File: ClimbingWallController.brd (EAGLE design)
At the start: 100 x 80 mm, 339 parts, among them IC1 74HCT138D, IC2 74HCT138D, IC3 PIC24FJ32GB004, IC4 SN74LV4052AD, IC5 SN74LV4052AD, IC6 TC1015, IC7 NCP1117, J1 PWR, Q1 DPBT8105, Q10 DPBT8105, Q11 DPBT8105, Q12 DPBT8105, Q13 DPBT8105, Q14 DPBT8105, Q15 DPBT8105, Q16 DPBT8105, Q17 NC, Q2 DPBT8105, Q3 DPBT8105, Q4 DPBT8105, Q5 DPBT8105, Q6 DPBT8105, Q7 DPBT8105, Q8 DPBT8105, Q9 DPBT8105, X1 MINI-USB-32005-201

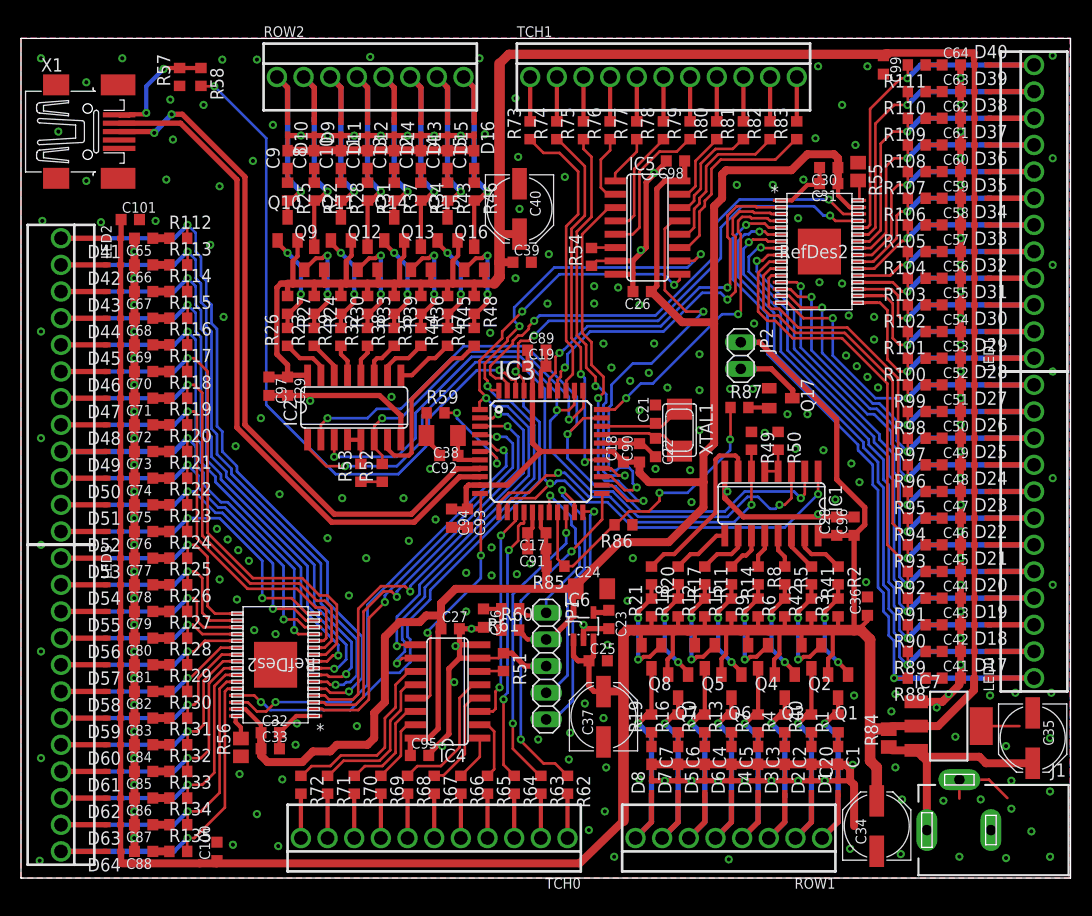
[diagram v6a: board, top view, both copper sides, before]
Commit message: DRC Passed with SEEED Rules. Added extra input to touch connector because 11-socket parts aren't available. Fixed 5v regulator pin out, and added PCB heat sink. Messed with device attributes for manufacturer part number. Exported BOM. (Awaiting clean up for BOM commit).
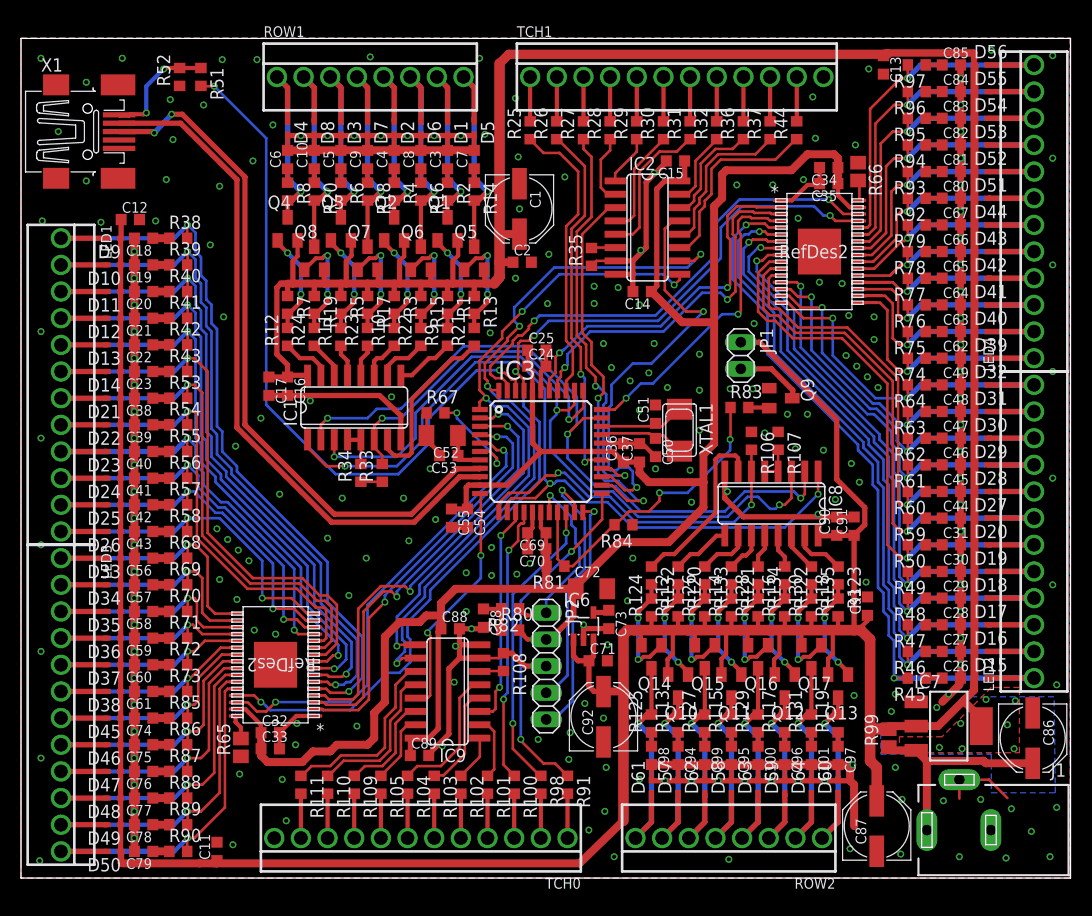
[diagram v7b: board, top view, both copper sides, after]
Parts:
- removed LED0: (no value), Parts:OSTVN12
- added LED4: (no value), Parts:OSTVN12
- C1: value 22n -> 100uF; device resistor:C0603 -> resistor:PANASONIC_D
- C10, C3, C4, C5, C6, C7, C8, C9: device resistor:C0603 -> resistor:C0603K
- C100, C101, C99: value 0.1uF -> 22n; device rcl:C0603K -> resistor:C0603K
- C11, C12, C13, C14: value 22n -> 0.1uF; device resistor:C0603 -> rcl:C0603K
- C15: value 22n -> NC; device resistor:C0603 -> rcl:C0603K
- C16, C90: value NC -> 0.1uF
- C17: value 0.1uF -> NC
- C18, C19, C26, C27, C28, C29, C31: value 0.1uF -> 1n; device rcl:C0603K -> resistor:C0603K
- C2: value 22n -> 1uF; device resistor:C0603 -> rcl:C0603K
- C20: value 22n -> 1n; device resistor:C0603 -> resistor:C0603K
- C21, C22: value NC -> 1n; device rcl:C0603K -> resistor:C0603K
- C23: value 470pF -> 1n; device rcl:C0603K -> resistor:C0603K
- C24: value 10uF -> 0.1uF; device rcl:C1206K -> rcl:C0603K
- C25: value 1uF -> NC
- C30, C39: value 1uF -> 1n; device rcl:C0603K -> resistor:C0603K
- C34: value 100uF -> 1uF; device resistor:PANASONIC_D -> rcl:C0603K
- C35: value 100uF -> 0.1uF; device resistor:PANASONIC_D -> rcl:C0603K
- C36: value 1uF -> 0.1uF
- C37: value 100uF -> NC; device resistor:PANASONIC_D -> rcl:C0603K
- C38: value 10uF -> 1n; device rcl:C1206K -> resistor:C0603K
- C40: value 100uF -> 1n; device resistor:PANASONIC_D -> resistor:C0603K
- C50, C51, C53, C55, C68, C70: value 1n -> NC; device resistor:C0603K -> rcl:C0603K
- C52, C72: value 1n -> 10uF; device resistor:C0603K -> rcl:C1206K
- C54, C69, C88: value 1n -> 0.1uF; device resistor:C0603K -> rcl:C0603K
- C71: value 1n -> 1uF; device resistor:C0603K -> rcl:C0603K
- C73: value 1n -> 470pF; device resistor:C0603K -> rcl:C0603K
- C86, C87: value 1n -> 100uF; device resistor:C0603K -> resistor:PANASONIC_D
- C92: value NC -> 100uF; device rcl:C0603K -> resistor:PANASONIC_D
- C93: value 0.1uF -> 1uF
- C94, C95, C96, C97, C98: value NC -> 22n; device rcl:C0603K -> resistor:C0603K
- IC2: value 74HCT138D -> SN74LV4052AD
- IC4, IC5: value SN74LV4052AD -> TLC5952; device Parts:SO16 -> Parts:HTSSOP-32POWERPAD
- IC7: value NCP1117 -> (none)
- IC8: value (none) -> 74HCT138D; device Parts:HTSSOP-32POWERPAD -> Parts:SO16
- IC9: value (none) -> SN74LV4052AD; device Parts:HTSSOP-32POWERPAD -> Parts:SO16
- J1: device con-jack:DCJ0303 -> Parts:DCJ0303
- JP1: value DEBUG -> BUZZER; device pinhead:1X05 -> pinhead:1X02
- JP2: value BUZZER -> DEBUG; device pinhead:1X02 -> pinhead:1X05
- Q17: value NC -> DPBT8105; device transistor:SOT23-EBC -> Parts:SOT23
- Q9: value DPBT8105 -> NC; device Parts:SOT23 -> transistor:SOT23-EBC
- R1, R13, R19, R7: value 20 -> NC
- R10, R22: value 20 -> 750
- R100, R101, R102, R103, R104, R105, R109, R110, R111, R91, R98: value 300 -> 390
- R106, R107, R108: value 300 -> 4.7k
- R112, R114, R116, R118, R124, R126, R128, R130: value 300 -> NC
- R113, R115, R117, R119, R125, R127, R129, R131: value 300 -> 20
- R12, R21, R24, R9: value NC -> 750
- R120, R121, R122, R123, R132, R133, R134, R135: value 300 -> 750
- R14, R2, R20, R8: value 750 -> 20
- R17, R5: value 750 -> NC
- R18, R6: value NC -> 20
- R25, R28, R31, R37: value 20 -> 390
- R26, R29, R32, R44: value 750 -> 390
- R27, R30, R36: value NC -> 390
- R33: value NC -> 4.7k
- R34: value 20 -> 4.7k
- R35: value 750 -> 4.7k
- R38, R41, R47: value 750 -> 300
- R39, R42, R45, R48, R85, R86, R87: value NC -> 300
- R40, R43, R46: value 20 -> 300
- R49, R50, R53, R54, R57, R58, R59, R60: value 4.7k -> 300
- R55, R56: value 1.37k 0.5% -> 300; device resistor:R0805 -> Parts:R0603
- R61, R62, R63, R64, R68, R69, R70, R71, R72, R73, R74, R75, R76, R77, R78, R79: value 390 -> 300
- R65, R66: value 390 -> 1.37k 0.5%; device Parts:R0603 -> resistor:R0805
- R67, R80: value 390 -> 4.7k
- R81, R83: value 390 -> NC
- R84: value 0 -> NC; device resistor:R0805 -> Parts:R0603
- R99: value 300 -> 0; device Parts:R0603 -> resistor:R0805
- TCH0, TCH1: device Parts:OSTVN11 -> Parts:OSTVN12
- moved C85 102.2 mm to (88.6, 77.5), turned to 0 degrees
- moved D38 99.0 mm to (8.89, 17.8), turned to 180 degrees
- moved D56 99.0 mm to (91.4, 77.5), turned to 0 degrees
- moved C84 99.0 mm to (88.6, 74.9), turned to 0 degrees
- moved D55 96.3 mm to (91.4, 74.9), turned to 0 degrees
- moved D37 96.3 mm to (8.89, 20.3), turned to 180 degrees
- moved C83 95.9 mm to (88.6, 72.4), turned to 0 degrees
- moved LED1 94.2 mm to (3.81, 47.0), turned to 270 degrees
- moved D36 93.8 mm to (8.89, 22.9), turned to 180 degrees
- moved D54 93.8 mm to (91.4, 72.4), turned to 0 degrees
- moved LED2 93.8 mm to (96.5, 33.0), turned to 90 degrees
- moved C61 92.9 mm to (11.7, 17.8), turned to 180 degrees
- moved C82 92.9 mm to (88.6, 69.8), turned to 0 degrees
- moved D35 91.5 mm to (8.89, 25.4), turned to 180 degrees
- moved D53 91.5 mm to (91.4, 69.8), turned to 0 degrees
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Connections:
- removed net N$118 (its old number): C67.1, R114.1
- removed net N$66: R65.2, TCH0.4
- removed net N$68: R67.2, TCH0.6
- removed net N$70: R69.2, TCH0.8
- removed net N$72: R71.2, TCH0.10
- removed net N$74: R74.2, TCH1.2
- removed net N$75: R76.2, TCH1.4
- removed net N$76: R78.2, TCH1.6
- removed net N$77: R80.2, TCH1.8
- removed net N$78: R82.2, TCH1.10
- new net N$31: R98.2, TCH0.2
- new net N$32: R101.2, TCH0.4
- new net N$34: C101.1, R131.1
- new net N$35: R103.2, TCH0.6
- new net N$36: R105.2, TCH0.8
- new net N$37: R110.2, TCH0.10
- new net N$38: R26.2, TCH1.2
- new net N$39: R28.2, TCH1.4
- new net N$40: R30.2, TCH1.6
- new net N$49: R37.2, TCH1.10
- net +3V3: now also C14.1, C15.1, C25.1, C34.1, C35.1, C36.1, C37.1, C54.1, C55.1, C69.1, C70.1, C72.1, C88.1, IC2.16, IC4.31, IC5.31, IC9.16, JP2.2, R80.2, R81.2; no longer C17.1, C18.1, C19.1, C26.1, C27.1, C30.1, C31.1, C90.1, C91.1, C93.1, C94.1, C95.1, C98.1, IC4.16, IC5.16, IC8.31, IC9.31, JP1.2, R60.2, R85.2
- net +5V: now also C1.+, C11.1, C12.1, C13.1, C16.1, C17.1, C2.1, C71.1, C87.+, C90.1, C91.1, C92.+, C93.1, D10.C, D11.C, D12.C, D13.C, D14.C, D15.C, D16.C, D9.C, IC7.4, IC8.16, JP1.1, Q17.2, R1.1, R112.1, R114.1, R116.1, R118.1, R124.1, R126.1, R128.1, R13.1, R130.1, R17.1, R19.1, R5.1, R7.1, R99.2; no longer C100.1, C101.1, C25.1, C28.1, C29.1, C34.+, C36.1, C37.+, C39.1, C40.+, C96.1, C97.1, C99.1, D57.C, D58.C, D59.C, D60.C, D61.C, D62.C, D63.C, D64.C, IC2.16, JP2.1, Q9.2, R12.1, R18.1, R21.1, R24.1, R27.1, R30.1, R33.1, R36.1, R39.1, R42.1, R45.1, R48.1, R6.1, R84.2, R9.1
- net AMSEL0: now also IC2.10, IC9.10; no longer IC4.10, IC5.10
- net AMSEL1: now also IC2.9, IC9.9; no longer IC4.9, IC5.9
- net B0: now also D17.A, IC5.7, LED2.3, R47.2; no longer D19.A, IC8.7, LED0.3, R90.2
- net B1: now also D20.A, IC5.10, LED2.6, R50.2; no longer D22.A, IC8.10, LED0.6, R93.2
- net B10: now also D23.A, IC4.13, LED1.9, R55.2; no longer D49.A, IC9.13, LED2.9, R120.2
- net B11: now also D26.A, IC4.16, LED1.12, R58.2; no longer D52.A, IC9.16, LED2.12, R123.2
- net B12: now also D35.A, IC4.19, R70.2; no longer D55.A, IC9.19, R126.2
- net B13: now also D38.A, IC4.22, R73.2; no longer D58.A, IC9.22, R129.2
- net B14: now also D47.A, IC4.25, R87.2; no longer D61.A, IC9.25, R132.2
- net B15: now also D50.A, IC4.28, R90.2; no longer D64.A, IC9.28, R135.2
- net B2: now also D29.A, IC5.13, LED2.9, R61.2; no longer D25.A, IC8.13, LED0.9, R96.2
- net B3: now also D32.A, IC5.16, LED2.12, R64.2; no longer D28.A, IC8.16, LED0.12, R99.2
- net B4: now also D41.A, IC5.19, LED4.3, R76.2; no longer D31.A, IC8.19, LED1.3, R102.2
- net B5: now also D44.A, IC5.22, LED4.6, R79.2; no longer D34.A, IC8.22, LED1.6, R105.2
- net B6: now also D53.A, IC5.25, LED4.9, R94.2; no longer D37.A, IC8.25, LED1.9, R108.2
- net B7: now also D56.A, IC5.28, LED4.12, R97.2; no longer D40.A, IC8.28, LED1.12, R111.2
- net B8: now also D11.A, IC4.7, LED1.3, R40.2; no longer D43.A, IC9.7, LED2.3, R114.2
- net B9: now also D14.A, IC4.10, LED1.6, R43.2; no longer D46.A, IC9.10, LED2.6, R117.2
- net C0_LAT: now also IC5.4; no longer IC8.4
- net C0_SCLK: now also IC5.3; no longer IC8.3
- net C0_SIN: now also IC5.2; no longer IC8.2
- net C0_SOUT: now also IC5.30; no longer IC8.30
- net C1_LAT: now also IC4.4; no longer IC9.4
- net C1_SCLK: now also IC4.3; no longer IC9.3
- net C1_SIN: now also IC4.2; no longer IC9.2
- net C1_SOUT: now also IC4.30; no longer IC9.30
- net CAIREF: now also IC5.32, R66.2; no longer IC8.32, R55.2
- net CAIREF1: now also IC4.32, R65.2; no longer IC9.32, R56.2
- net C_BLANK: now also IC4.29, IC5.29; no longer IC8.29, IC9.29
- net DISVREG: now also R67.2; no longer R59.2
- net G0: now also D16.A, IC5.6, LED2.2, R46.2; no longer D18.A, IC8.6, LED0.2, R89.2
- net G1: now also D19.A, IC5.9, LED2.5, R49.2; no longer D21.A, IC8.9, LED0.5, R92.2
- net G10: now also D22.A, IC4.12, LED1.8, R54.2; no longer D48.A, IC9.12, LED2.8, R119.2
- net G11: now also D25.A, IC4.15, LED1.11, R57.2; no longer D51.A, IC9.15, LED2.11, R122.2
- net G12: now also D34.A, IC4.18, R69.2; no longer D54.A, IC9.18, R125.2
- net G13: now also D37.A, IC4.21, R72.2; no longer D57.A, IC9.21, R128.2
- net G14: now also D46.A, IC4.24, R86.2; no longer D60.A, IC9.24, R131.2
- net G15: now also D49.A, IC4.27, R89.2; no longer D63.A, IC9.27, R134.2
- net G2: now also D28.A, IC5.12, LED2.8, R60.2; no longer D24.A, IC8.12, LED0.8, R95.2
- net G3: now also D31.A, IC5.15, LED2.11, R63.2; no longer D27.A, IC8.15, LED0.11, R98.2
- net G4: now also D40.A, IC5.18, LED4.2, R75.2; no longer D30.A, IC8.18, LED1.2, R101.2
- net G5: now also D43.A, IC5.21, LED4.5, R78.2; no longer D33.A, IC8.21, LED1.5, R104.2
- net G6: now also D52.A, IC5.24, LED4.8, R93.2; no longer D36.A, IC8.24, LED1.8, R107.2
- net G7: now also D55.A, IC5.27, LED4.11, R96.2; no longer D39.A, IC8.27, LED1.11, R110.2
- net G8: now also D10.A, IC4.6, LED1.2, R39.2; no longer D42.A, IC9.6, LED2.2, R113.2
- net G9: now also D13.A, IC4.9, LED1.5, R42.2; no longer D45.A, IC9.9, LED2.5, R116.2
- net GND: now also C1.-, C34.2, C35.2, C37.2, C40.2, C86.-, C87.-, C92.-, D57.A, D58.A, D59.A, D60.A, D61.A, D62.A, D63.A, D64.A, IC2.7, IC4.1, IC4.33, IC5.1, IC5.33, IC8.8, IC9.7, IC9.8, JP2.3, Q9.E, R106.1, R107.1, R108.1, R33.1, R34.1, R35.1, R65.1, R66.1, R67.1, R84.1, TCH0.12, TCH1.12; no longer C1.2, C34.-, C35.-, C37.-, C40.-, C86.2, C87.2, C92.2, D10.A, D11.A, D12.A, D13.A, D14.A, D15.A, D16.A, D9.A, IC4.7, IC4.8, IC5.7, IC5.8, IC7.4, IC8.1, IC8.33, IC9.1, IC9.33, JP1.3, Q17.E, R49.1, R50.1, R51.1, R53.1, R54.1, R55.1, R56.1, R57.1, R59.1, R86.1
- net MCLR_: now also JP2.1, R82.1; no longer JP1.1, R61.1
- net N$1: now also Q13.1, R118.2, R123.2; no longer Q1.1, R2.2, R3.2
- net N$10: now also C95.1, R115.1; no longer C5.1, R13.1
- net N$100: now also C49.1, R64.1; no longer C52.1, R99.1
- net N$101: now also C62.1, R74.1; no longer C53.1, R100.1
- net N$102: now also C63.1, R75.1; no longer C54.1, R101.1
- net N$103: now also C64.1, R76.1; no longer C55.1, R102.1
- net N$104: now also C65.1, R77.1; no longer C56.1, R103.1
- net N$105: now also C66.1, R78.1; no longer C57.1, R104.1
- net N$106: now also C67.1, R79.1; no longer C58.1, R105.1
- net N$107: now also C80.1, R92.1; no longer C59.1, R106.1
- net N$108: now also C81.1, R93.1; no longer C60.1, R107.1
- net N$109: now also C82.1, R94.1; no longer C61.1, R108.1
- net N$11: now also Q10.1, R112.2, R120.2; no longer Q7.1, R17.2, R18.2
- net N$110: now also C83.1, R95.1; no longer C62.1, R109.1
- net N$111: now also C84.1, R96.1; no longer C63.1, R110.1
- net N$112: now also C85.1, R97.1; no longer C64.1, R111.1
- net N$114: now also C18.1, R38.1; no longer C65.1, R112.1
- net N$116: now also C19.1, R39.1; no longer C66.1, R113.1
- net N$12: now also C94.1, R113.1; no longer C6.1, R16.1
- net N$120: now also C21.1, R41.1; no longer C68.1, R115.1
- net N$122: now also C22.1, R42.1; no longer C69.1, R116.1
- net N$124: now also C23.1, R43.1; no longer C70.1, R117.1
- net N$126: now also C38.1, R53.1; no longer C71.1, R118.1
- net N$128: now also C39.1, R54.1; no longer C72.1, R119.1
- net N$13: now also Q14.1, R124.2, R132.2; no longer Q8.1, R20.2, R21.2
- net N$130: now also C40.1, R55.1; no longer C73.1, R120.1
- net N$132: now also C41.1, R56.1; no longer C74.1, R121.1
- net N$134: now also C42.1, R57.1; no longer C75.1, R122.1
- net N$136: now also C43.1, R58.1; no longer C76.1, R123.1
- net N$138: now also C56.1, R68.1; no longer C77.1, R124.1
- net N$14: now also C98.1, R125.1; no longer C7.1, R19.1
- net N$140: now also C57.1, R69.1; no longer C78.1, R125.1
- net N$142: now also C58.1, R70.1; no longer C79.1, R126.1
- net N$144: now also C59.1, R71.1; no longer C80.1, R127.1
- net N$146: now also C60.1, R72.1; no longer C81.1, R128.1
- net N$148: now also C61.1, R73.1; no longer C82.1, R129.1
- net N$15: now also Q8.1, R19.2; no longer Q9.1, R23.2
- net N$150: now also C74.1, R85.1; no longer C83.1, R130.1
- net N$152: now also C75.1, R86.1; no longer C84.1, R131.1
- net N$154: now also C76.1, R87.1; no longer C85.1, R132.1
- net N$156: now also C77.1, R88.1; no longer C86.1, R133.1
- net N$158: now also C78.1, R89.1; no longer C87.1, R134.1
- net N$16: now also C10.1, R20.1; no longer C8.1, R22.1
- net N$160: now also C79.1, R90.1; no longer C88.1, R135.1
- net N$17: now also Q4.1, R12.2, R7.2; no longer Q10.1, R26.2, R27.2
- net N$18: now also C6.1, R8.1; no longer C9.1, R25.1
- net N$19: now also Q3.1, R11.2, R5.2; no longer Q11.1, R29.2, R30.2
- net N$2: now also C97.1, R119.1; no longer C1.1, R1.1
- net N$20: now also C5.1, R6.1; no longer C10.1, R28.1
- net N$21: now also Q7.1, R17.2, R23.2; no longer Q12.1, R32.2, R33.2
- net N$22: now also C9.1, R18.1; no longer C11.1, R31.1
- net N$23: now also Q6.1, R15.2, R22.2; no longer Q13.1, R35.2, R36.2
- net N$24: now also C8.1, R16.1; no longer C12.1, R34.1
- net N$25: now also Q2.1, R10.2, R3.2; no longer Q14.1, R38.2, R39.2
- net N$26: now also C4.1, R4.1; no longer C13.1, R37.1
- net N$27: now also Q1.1, R1.2, R9.2; no longer Q15.1, R44.2, R45.2
- net N$28: now also C3.1, R2.1; no longer C14.1, R43.1
- net N$29: now also Q5.1, R13.2, R21.2; no longer Q16.1, R47.2, R48.2
- net N$3: now also Q12.1, R116.2, R122.2; no longer Q3.1, R5.2, R6.2
- net N$30: now also C7.1, R14.1; no longer C15.1, R46.1
- net N$33: now also Q17.1, R130.2, R135.2; no longer Q2.1, R41.2, R42.2
- net N$4: now also C96.1, R117.1; no longer C2.1, R4.1
- net N$41: now also IC8.4, IC8.5, R107.2; no longer IC1.4, IC1.5, R50.2
- net N$42: now also IC9.6, R108.2; no longer IC4.6, R51.2
- net N$43: now also IC1.4, IC1.5, R34.2; no longer IC2.4, IC2.5, R53.2
- net N$44: now also IC2.6, R35.2; no longer IC5.6, R54.2
- net N$45: now also R51.2; no longer R58.2
- net N$46: now also C68.1, R80.1, R82.2; no longer C16.1, R60.1, R61.2
- net N$47: now also R91.2; no longer R62.2
- net N$48: now also R32.2, TCH1.8; no longer R63.2, TCH0.2
- net N$5: now also Q16.1, R128.2, R134.2; no longer Q4.1, R8.2, R9.2
- net N$6: now also C100.1, R129.1; no longer C3.1, R7.1
- net N$65: now also R100.2; no longer R64.2
- net N$67: now also R102.2; no longer R66.2
- net N$69: now also R104.2; no longer R68.2
- net N$7: now also Q15.1, R126.2, R133.2; no longer Q5.1, R11.2, R12.2
- net N$71: now also R109.2; no longer R70.2
- net N$73: now also R111.2; no longer R72.2
- net N$79: now also R25.2; no longer R73.2
- net N$8: now also C99.1, R127.1; no longer C4.1, R10.1
- net N$80: now also R27.2; no longer R75.2
- net N$81: now also R29.2; no longer R77.2
- net N$82: now also R31.2; no longer R79.2
- net N$83: now also R36.2; no longer R81.2
- net N$84: now also R44.2; no longer R83.2
- net N$85: now also C73.1; no longer C23.1
- net N$87: now also Q9.B, R83.2; no longer Q17.B, R87.2
- net N$88: now also JP1.2, Q9.C; no longer JP2.2, Q17.C
- net N$89: now also C26.1, R45.1; no longer C41.1, R88.1
- net N$9: now also Q11.1, R114.2, R121.2; no longer Q6.1, R14.2, R15.2
- net N$90: now also C27.1, R46.1; no longer C42.1, R89.1
- net N$91: now also C28.1, R47.1; no longer C43.1, R90.1
- net N$92: now also C29.1, R48.1; no longer C44.1, R91.1
- net N$93: now also C30.1, R49.1; no longer C45.1, R92.1
- net N$94: now also C31.1, R50.1; no longer C46.1, R93.1
- net N$95: now also C44.1, R59.1; no longer C47.1, R94.1
- net N$96: now also C45.1, R60.1; no longer C48.1, R95.1
- net N$97: now also C46.1, R61.1; no longer C49.1, R96.1
- net N$98: now also C47.1, R62.1; no longer C50.1, R97.1
- net N$99: now also C48.1, R63.1; no longer C51.1, R98.1
- net OSCI: now also C50.1; no longer C22.1
- net OSCO: now also C51.1; no longer C21.1
- net PGEC: now also JP2.5; no longer JP1.5
- net PGED: now also JP2.4; no longer JP1.4
- net R0: now also D15.A, IC5.5, LED2.1, R45.2; no longer D17.A, IC8.5, LED0.1, R88.2
- net R1: now also D18.A, IC5.8, LED2.4, R48.2; no longer D20.A, IC8.8, LED0.4, R91.2
- net R10: now also D21.A, IC4.11, LED1.7, R53.2; no longer D47.A, IC9.11, LED2.7, R118.2
- net R11: now also D24.A, IC4.14, LED1.10, R56.2; no longer D50.A, IC9.14, LED2.10, R121.2
- net R12: now also D33.A, IC4.17, R68.2; no longer D53.A, IC9.17, R124.2
- net R13: now also D36.A, IC4.20, R71.2; no longer D56.A, IC9.20, R127.2
- net R14: now also D45.A, IC4.23, R85.2; no longer D59.A, IC9.23, R130.2
- net R15: now also D48.A, IC4.26, R88.2; no longer D62.A, IC9.26, R133.2
- net R2: now also D27.A, IC5.11, LED2.7, R59.2; no longer D23.A, IC8.11, LED0.7, R94.2
- net R3: now also D30.A, IC5.14, LED2.10, R62.2; no longer D26.A, IC8.14, LED0.10, R97.2
- net R4: now also D39.A, IC5.17, LED4.1, R74.2; no longer D29.A, IC8.17, LED1.1, R100.2
- net R5: now also D42.A, IC5.20, LED4.4, R77.2; no longer D32.A, IC8.20, LED1.4, R103.2
- net R6: now also D51.A, IC5.23, LED4.7, R92.2; no longer D35.A, IC8.23, LED1.7, R106.2
- net R7: now also D54.A, IC5.26, LED4.10, R95.2; no longer D38.A, IC8.26, LED1.10, R109.2
- net R8: now also D9.A, IC4.5, LED1.1, R38.2; no longer D41.A, IC9.5, LED2.1, R112.2
- net R9: now also D12.A, IC4.8, LED1.4, R41.2; no longer D44.A, IC9.8, LED2.4, R115.2
- net RAEN: now also IC8.6, R106.2; no longer IC1.6, R49.2
- net RBEN: now also IC1.6, R33.2; no longer IC2.6, R52.2
- net ROW0: now also D60.C, Q13.3, R119.2, ROW2.1; no longer D1.C, Q1.3, R1.2, ROW1.1
- net ROW0EN_: now also IC8.15, R123.1; no longer IC1.15, R2.1
- net ROW1: now also D64.C, Q17.3, R131.2, ROW2.2; no longer D2.C, Q2.3, R40.2, ROW1.2
- net ROW10: now also D3.C, Q3.3, R6.2, ROW1.3; no longer D11.C, Q11.3, R28.2, ROW2.3
- net ROW10EN_: now also IC1.13, R11.1; no longer IC2.13, R29.1
- net ROW11: now also D7.C, Q7.3, R18.2, ROW1.4; no longer D12.C, Q12.3, R31.2, ROW2.4
- net ROW11EN_: now also IC1.12, R23.1; no longer IC2.12, R32.1
- net ROW12: now also D2.C, Q2.3, R4.2, ROW1.5; no longer D14.C, Q14.3, R37.2, ROW2.5
- net ROW12EN_: now also IC1.11, R10.1; no longer IC2.11, R38.1
- net ROW13: now also D6.C, Q6.3, R16.2, ROW1.6; no longer D13.C, Q13.3, R34.2, ROW2.6
- net ROW13EN_: now also IC1.10, R22.1; no longer IC2.10, R35.1
- net ROW14: now also D1.C, Q1.3, R2.2, ROW1.7; no longer D15.C, Q15.3, R43.2, ROW2.7
- net ROW14EN_: now also IC1.9, R9.1; no longer IC2.9, R44.1
- net ROW15: now also D5.C, Q5.3, R14.2, ROW1.8; no longer D16.C, Q16.3, R46.2, ROW2.8
- net ROW15EN_: now also IC1.7, R21.1; no longer IC2.7, R47.1
- net ROW1EN_: now also IC8.14, R135.1; no longer IC1.14, R41.1
- net ROW2: now also D59.C, Q12.3, R117.2, ROW2.3; no longer D3.C, Q3.3, R4.2, ROW1.3
- net ROW2EN_: now also IC8.13, R122.1; no longer IC1.13, R5.1
- net ROW3: now also D63.C, Q16.3, R129.2, ROW2.4; no longer D4.C, Q4.3, R7.2, ROW1.4
- net ROW3EN_: now also IC8.12, R134.1; no longer IC1.12, R8.1
- net ROW4: now also D58.C, Q11.3, R115.2, ROW2.5; no longer D6.C, Q6.3, R13.2, ROW1.5
- net ROW4EN_: now also IC8.11, R121.1; no longer IC1.11, R14.1
- net ROW5: now also D62.C, Q15.3, R127.2, ROW2.6; no longer D5.C, Q5.3, R10.2, ROW1.6
- net ROW5EN_: now also IC8.10, R133.1; no longer IC1.10, R11.1
- net ROW6: now also D57.C, Q10.3, R113.2, ROW2.7; no longer D7.C, Q7.3, R16.2, ROW1.7
- net ROW6EN_: now also IC8.9, R120.1; no longer IC1.9, R17.1
- net ROW7: now also D61.C, Q14.3, R125.2, ROW2.8; no longer D8.C, Q8.3, R19.2, ROW1.8
- net ROW7EN_: now also IC8.7, R132.1; no longer IC1.7, R20.1
- net ROW8: now also D4.C, Q4.3, R8.2, ROW1.1; no longer D10.C, Q10.3, R25.2, ROW2.1
- net ROW8EN_: now also IC1.15, R12.1; no longer IC2.15, R26.1
- net ROW9: now also D8.C, Q8.3, R20.2, ROW1.2; no longer D9.C, Q9.3, R22.2, ROW2.2
- net ROW9EN_: now also IC1.14, R24.1; no longer IC2.14, R23.1
- net RSEL0: now also IC8.1; no longer IC2.1
- net RSEL1: now also IC8.2; no longer IC2.2
- net RSEL2: now also IC8.3; no longer IC2.3
- net TMUX0: now also IC9.3; no longer IC4.3
- net TMUX1: now also IC9.13; no longer IC4.13
- net TMUX2: now also IC2.3; no longer IC5.3
- net TMUX3: now also IC2.13; no longer IC5.13
- net TOUCH0: now also R91.1; no longer R62.1
- net TOUCH1: now also R98.1; no longer R63.1
- net TOUCH10: now also IC9.11, R111.1; no longer IC4.11, R72.1
- net TOUCH11: now also R25.1; no longer R73.1
- net TOUCH12: now also R26.1; no longer R74.1
- net TOUCH13: now also R27.1; no longer R75.1
- net TOUCH14: now also IC2.2, R28.1; no longer IC5.2, R76.1
- net TOUCH15: now also IC2.1, R29.1; no longer IC5.1, R77.1
- net TOUCH16: now also IC2.4, R30.1; no longer IC5.4, R78.1
- net TOUCH17: now also IC2.5, R31.1; no longer IC5.5, R79.1
- net TOUCH18: now also IC2.15, R32.1; no longer IC5.15, R80.1
- net TOUCH19: now also IC2.14, R36.1; no longer IC5.14, R81.1
- net TOUCH2: now also R100.1; no longer R64.1
- net TOUCH20: now also IC2.12, R37.1; no longer IC5.12, R82.1
- net TOUCH21: now also IC2.11, R44.1; no longer IC5.11, R83.1
- net TOUCH3: now also IC9.2, R101.1; no longer IC4.2, R65.1
- net TOUCH4: now also IC9.1, R102.1; no longer IC4.1, R66.1
- net TOUCH5: now also IC9.4, R103.1; no longer IC4.4, R67.1
- net TOUCH6: now also IC9.5, R104.1; no longer IC4.5, R68.1
- net TOUCH7: now also IC9.15, R105.1; no longer IC4.15, R69.1
- net TOUCH8: now also IC9.14, R109.1; no longer IC4.14, R70.1
- net TOUCH9: now also IC9.12, R110.1; no longer IC4.12, R71.1
- net V+: now also C86.+, R99.1; no longer C35.+, R84.1
- net VBUS: now also R51.1, R52.2; no longer R57.2, R58.1
- net VDDCORE: now also C52.1, C53.1; no longer C38.1, C92.1
- net VREF+: now also R81.1, R83.1, R84.2; no longer R85.1, R86.2, R87.1
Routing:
- net GND: track 351.9 -> 345.3 mm, vias 232 -> 225
- net N$78: track 4.23 -> 0.00 mm
- net N$77: track 4.23 -> 0.00 mm
- net N$76: track 4.23 -> 0.00 mm
- net N$75: track 4.23 -> 0.00 mm
- net N$74: track 4.23 -> 0.00 mm
- net N$49: track 0.00 -> 4.23 mm
- net N$40: track 0.00 -> 4.23 mm
- net N$39: track 0.00 -> 4.23 mm
- net N$38: track 0.00 -> 4.23 mm
- net N$72: track 4.23 -> 0.00 mm
- net N$70: track 4.23 -> 0.00 mm
- net N$68: track 4.23 -> 0.00 mm
- net N$66: track 4.23 -> 0.00 mm
- net N$37: track 0.00 -> 4.23 mm
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- added copper zone on layer 1, net +5V
- added copper zone on layer 16, net +5V
